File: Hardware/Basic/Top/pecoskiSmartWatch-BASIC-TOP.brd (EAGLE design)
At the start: 38 x 38 mm, 29 parts, among them U2 NRF52832_MODULE_MDBT42

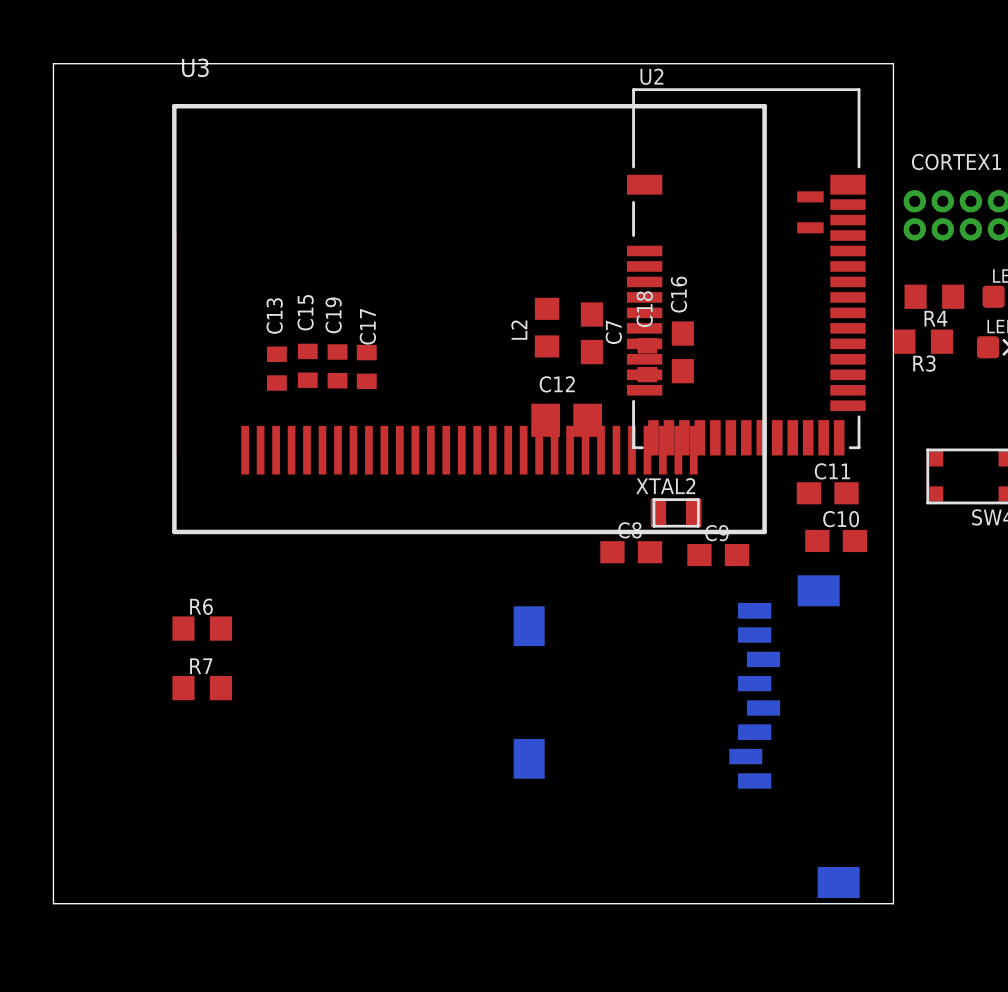
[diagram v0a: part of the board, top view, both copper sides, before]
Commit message: Updated top board hardware Eagle
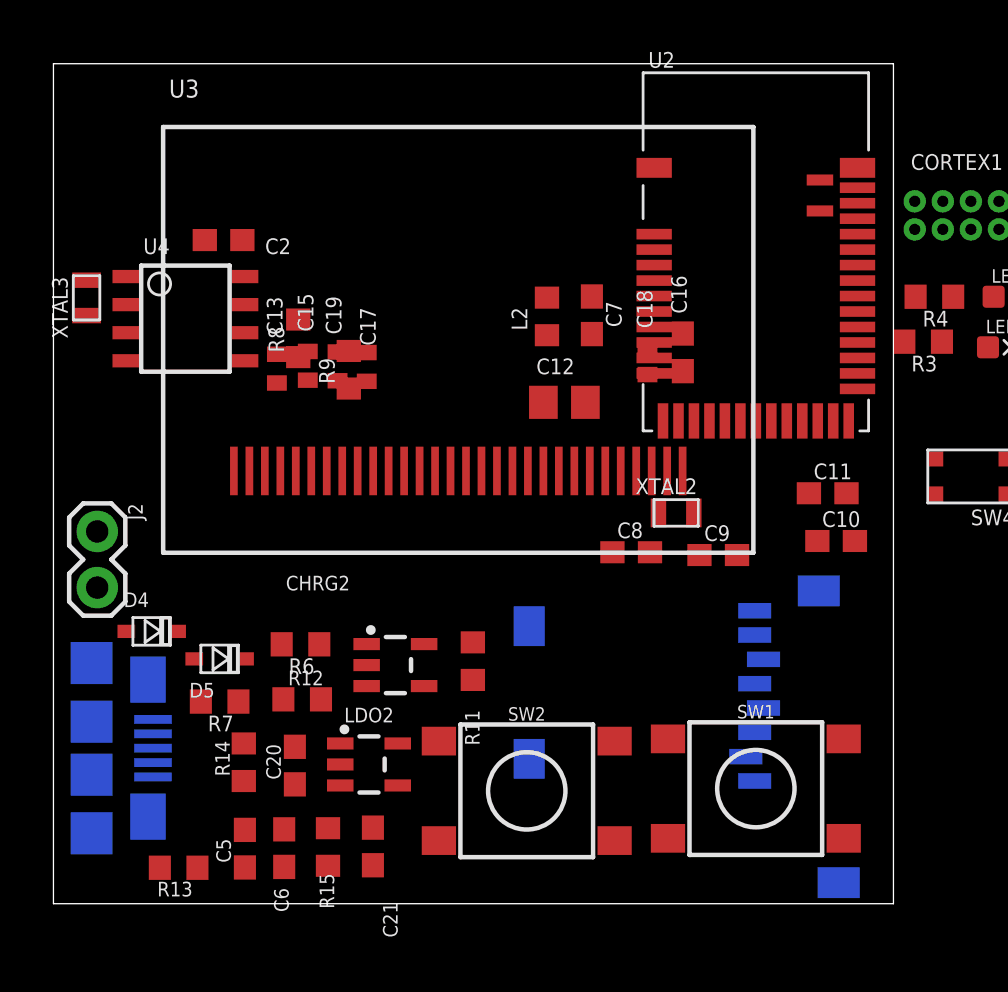
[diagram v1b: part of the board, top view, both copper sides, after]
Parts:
- added C2, C5, C6: 1u, LinnesLab-Passives:C0603
- added C20, C21: 4.7u, LinnesLab-Passives:C0603
- added CHRG2: MCP73831, LinnesLab-Power:SOT23-5
- added D4, D5: (no value), LinnesLab-DiscreteSemi:USC
- added J2: (no value), LinnesLab-Connectors:1X02
- added LDO2: MIC5504, LinnesLab-Power:SOT23-5
- added R11: (no value), LinnesLab-Passives:R0603
- added R12, R13, R14, R15: 100k, LinnesLab-Passives:R0603
- added R8, R9: 10k, LinnesLab-Passives:R0603
- added SW1, SW2: SWITCH.MOM, LinnesLab-Switches:TACTILE_SWITCH_SMD_6.2MM_TALL
- added U4: PCF8523, LinnesLab-Clocks:SO8
- added USB2: USB.MICRO-BIGGERPADS, LinnesLab-Connectors:USB-MICRO-01.BIGGERPADS
- added XTAL3: 32.7680kHz, LinnesLab-Clocks:2-SMD.NOLEAD.2.0MMTO1.2MM
- moved R6 4.50 mm to (11.2, 11.7), turned to 180 degrees
- moved U3 1.07 mm to (18.3, 20.8)
- moved R7 1.00 mm to (7.52, 9.14), turned to 180 degrees
- moved U2 0.88 mm to (31.8, 29.5)
- moved C12 0.82 mm to (23.1, 22.7)
- moved C7 0.81 mm to (24.4, 26.6)
- moved L2 0.51 mm to (22.3, 26.6)
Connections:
- new net BATT: R13.1, R14.2
- new net CHRG.STAT: CHRG2.1, R12.1
- new net N$17: CHRG2.5, R11.2
- new net N$19: U4.2, XTAL3.P$1
- new net N$20: U4.1, XTAL3.P$2
- new net SW1: SW1.A1, SW2.A1
- new net USB+: USB2.3
- new net USB-: USB2.2
- new net VBAT: U4.3
- new net VIN: C21.2, C5.2, CHRG2.4, D4.-, D5.-, LDO2.1, LDO2.3, R12.2
- new net VLIPO: C20.1, CHRG2.3, D4.+, J2.2, R13.2
- new net V_USB: D5.+, USB2.1
- net 3.3V: now also C2.1, C6.1, LDO2.5, R15.2, R8.2, R9.2, U4.8
- net GND: now also C2.2, C20.2, C21.1, C5.1, C6.2, CHRG2.2, J2.1, LDO2.2, R11.1, R14.1, R15.1, SW1.B1, SW1.B2, SW2.B1, SW2.B2, U4.4, USB2.5, USB2.S1, USB2.S2, USB2.S3, USB2.S4, USB2.S5, USB2.S6
- net SCL: now also R8.1, U4.6
- net SDA: now also R9.1, U4.5

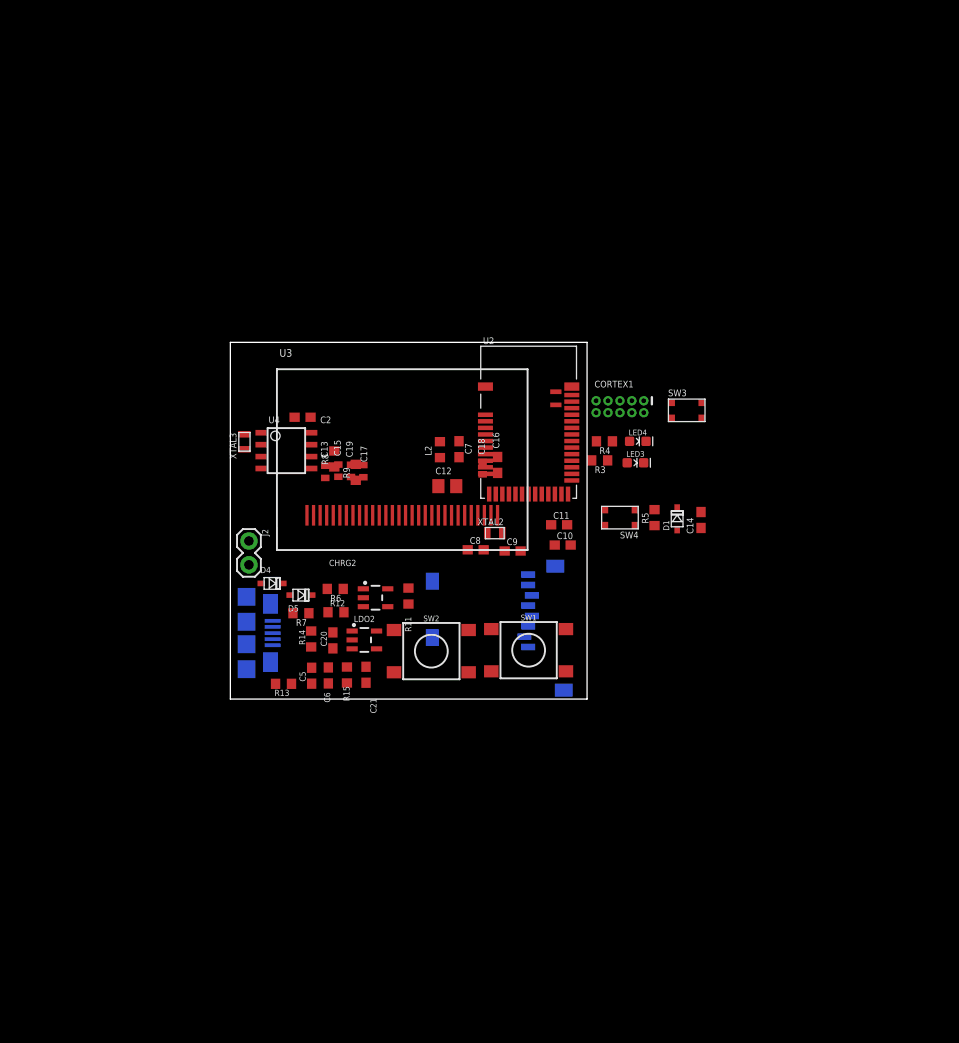
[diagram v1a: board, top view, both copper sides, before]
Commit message: Updated Eagle Hardware 2021_02_27
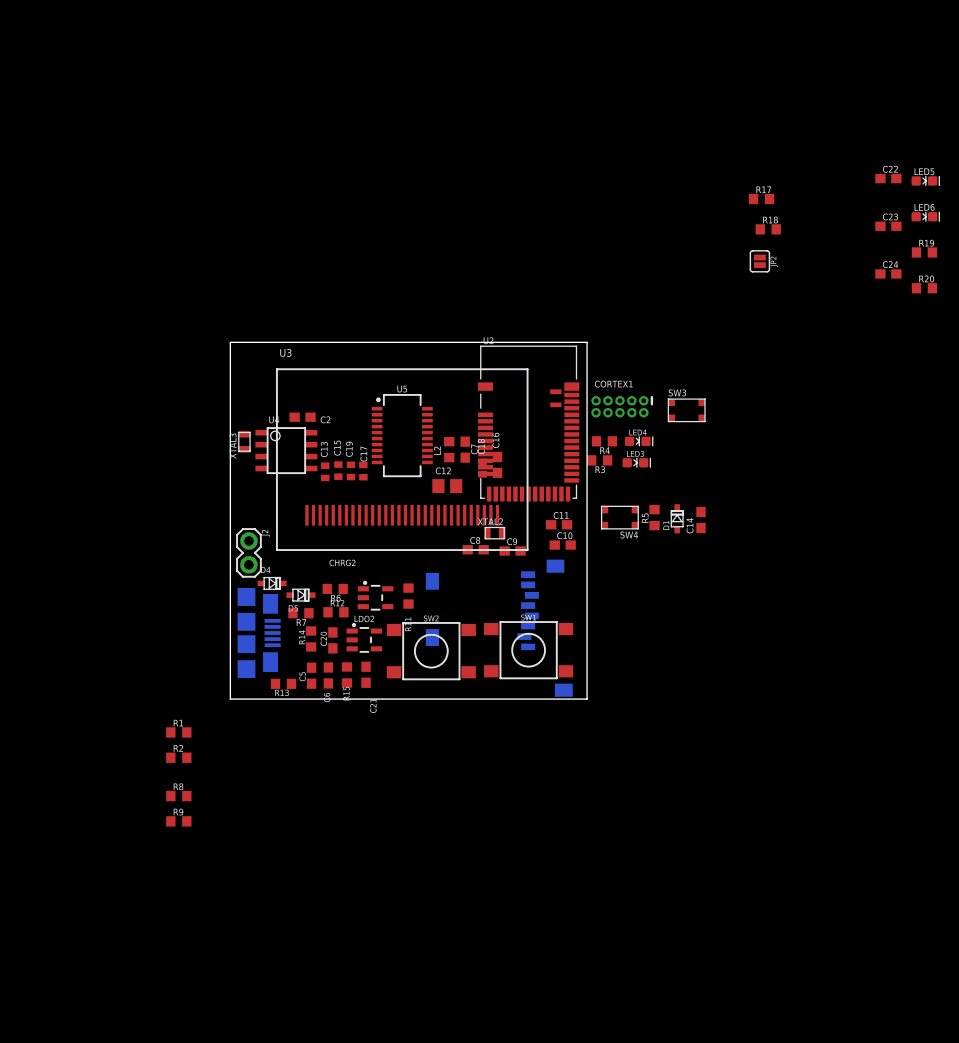
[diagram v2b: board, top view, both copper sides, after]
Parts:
- added C22: 100n, LinnesLab-Passives:C0603
- added C23, C24: 47p, LinnesLab-Passives:C0603
- added JP2: (no value), LinnesLab-Switches:SMT-JUMPER_2_NO_SILK
- added LED5: RED, LinnesLab-LED:LED-0603
- added LED6: YELLOW, LinnesLab-LED:LED-0603
- added R1, R2: 0, LinnesLab-Passives:R0603
- added R17, R18: 27, LinnesLab-Passives:R0603
- added R19, R20: 1k, LinnesLab-Passives:R0603
- added U5: FT231XS, LinnesLab-DigitalIC:SSOP20_L
- moved R9 41.7 mm to (-5.49, -13.0), turned to 0 degrees
- moved R8 39.5 mm to (-5.49, -10.3), turned to 0 degrees
- moved L2 0.99 mm to (23.3, 26.6)
- moved C7 0.66 mm to (25.0, 26.6)
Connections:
- removed net BATT: R13.1, R14.2
- removed net CD1: SD2.CD1
- removed net CHRG.STAT: CHRG2.1, R12.1
- removed net CS.OLED: U3.13
- removed net DC.OLED: U3.15
- removed net RESET.OLED: U3.14
- removed net RXD: U2.21
- removed net SD.CS: SD2.2
- removed net SW1: SW1.A1, SW2.A1
- removed net TXD: U2.19
- new net !CTS: JP2.2, U5.9
- new net !DTR: U5.1
- new net A4/BATT: R13.1, R14.2, U2.5
- new net A6/TIA: U2.7
- new net A7/PPG: U2.8
- new net D11/SW1: SW1.A1, U2.25
- new net D15/SW2: SW2.A1, U2.29
- new net D16/CS.OLED: U2.30, U3.13
- new net D27/CHRG.STATUS: CHRG2.1, R12.1, U2.4
- new net D29/LED.CTRL: U2.6
- new net D3/RESET.OLED: U2.16, U3.14
- new net D4/DC.OLED: U2.17, U3.15
- new net D5/CD1: SD2.CD1, U2.18
- new net D7/SD.CS: SD2.2, U2.20
- new net FT3V3: U5.13
- new net N$23: R17.2, U5.12
- new net N$24: R18.2, U5.11
- new net N$25: LED5.C, R19.2
- new net N$26: LED6.C, R20.2
- new net RXD.FT: R2.1, U5.4
- new net RXD.NRF: R1.2, U2.21
- new net RXLED: R19.1, U5.17
- new net TXD.FT: R1.1, U5.20
- new net TXD.NRF: R2.2, U2.19
- new net TXLED: R20.1, U5.10
- net 3.3V: now also C22.2, LED5.A, LED6.A, U5.14, U5.3
- net GND: now also C22.1, C23.2, C24.1, JP2.1, U5.16, U5.6
- net SCL: now also R9.1; no longer R8.1
- net SDA: now also R8.1; no longer R9.1
- net USB+: now also C23.1, R18.1
- net USB-: now also C24.2, R17.1
- net V_USB: now also U5.15

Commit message: HW Updates 2021/03/06
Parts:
- removed C22: 100n, LinnesLab-Passives:C0603
- removed C23, C24: 47p, LinnesLab-Passives:C0603
- removed CHRG2: MCP73831, LinnesLab-Power:SOT23-5
- removed CORTEX1: CORTEX_DEBUG_PTH, LinnesLab-Connectors:2X5-PTH-1.27MM
- removed D4, D5: (no value), LinnesLab-DiscreteSemi:USC
- removed JP2: (no value), LinnesLab-Switches:SMT-JUMPER_2_NO_SILK
- removed L2: 10u, LinnesLab-Passives:L0603
- removed LDO2: MIC5504, LinnesLab-Power:SOT23-5
- removed LED5: RED, LinnesLab-LED:LED-0603
- removed LED6: YELLOW, LinnesLab-LED:LED-0603
- removed R19, R20: 1k, LinnesLab-Passives:R0603
- removed U5: FT231XS, LinnesLab-DigitalIC:SSOP20_L
- removed XTAL3: 32.7680kHz, LinnesLab-Clocks:2-SMD.NOLEAD.2.0MMTO1.2MM
- added C1: 1u, LinnesLab-Passives:C0603
- added C3: (no value), LinnesLab-Passives:C0603
- added C4: 4.7u, LinnesLab-Passives:C0603
- added CHRG: MCP73831, LinnesLab-Power:SOT23-5
- added D2, D3: (no value), LinnesLab-DiscreteSemi:USC
- added DEBUG1: CORTEX_DEBUG_PTH, LinnesLab-Connectors:2X5-PTH-1.27MM
- added J1: (no value), LinnesLab-Connectors:1X02
- added JP1: (no value), LinnesLab-Switches:SMT-JUMPER_2_NO_SILK
- added L1: 10u, LinnesLab-Passives:L0603
- added LDO1: MIC5504, LinnesLab-Power:SOT23-5
- added LED1: RED, LinnesLab-LED:LED-0603
- added LED2: BLUE, LinnesLab-LED:LED-0603
- added R10: 10k, LinnesLab-Passives:R0603
- added R16: 1k, LinnesLab-Passives:R0603
- added U1: NRF52832_MODULE_MDBT42, LinnesLab-Microcontrollers:BLE_MODULE_RAYTAC_MDBT42
- added XTAL1: 32.768kHz, LinnesLab-Clocks:2-SMD.NOLEAD.2.0MMTO1.2MM
- C10: value 300p -> 4.7u
- C11: value 300p -> 100n
- C12: value 10u -> 47p; device LinnesLab-Passives:C0805 -> LinnesLab-Passives:C0603
- C13: value 2.2uF -> 47p; device LinnesLab-Passives:C0402 -> LinnesLab-Passives:C0603
- C14: value 100n -> 10uF
- C15: value 2.2uF -> 100n; device LinnesLab-Passives:C0402 -> LinnesLab-Passives:C0603
- C16: value 10uF -> 2.2uF; device LinnesLab-Passives:C0603 -> LinnesLab-Passives:C0402
- C2: value 1u -> 10u; device LinnesLab-Passives:C0603 -> LinnesLab-Passives:C0805
- C20: value 4.7u -> 2.2uF; device LinnesLab-Passives:C0603 -> LinnesLab-Passives:C0402
- C21: value 4.7u -> 1u
- C5: value 1u -> (none)
- C7: value 1u -> 300p
- C8: value (none) -> 300p
- C9: value (none) -> 1u
- J2: device LinnesLab-Connectors:1X02 -> LinnesLab-Connectors:1X07_1.27MM
- LED4: value BLUE -> YELLOW
- R1, R2: value 0 -> 10k
- R11: value (none) -> 10k
- R12, R13: value 100k -> 27
- R14: value 100k -> 390k
- R15: value 100k -> 1k
- R17, R18: value 27 -> 0
- R3: value 1k -> 100k
- R4: value 1k -> (none)
- R5, R8, R9: value 10k -> 100k
- R6: value 10k -> 1k
- R7: value 390k -> 1k
- SW1, SW2: value SWITCH.MOM -> (none); device LinnesLab-Switches:TACTILE_SWITCH_SMD_6.2MM_TALL -> LinnesLab-Switches:BUTTON-GULLWING
- SW3, SW4: value (none) -> SWITCH.MOM; device LinnesLab-Switches:BUTTON-GULLWING -> LinnesLab-Switches:TACTILE_SWITCH_SMD_6.2MM_TALL
- U2: value NRF52832_MODULE_MDBT42 -> PCF8523; device LinnesLab-Microcontrollers:BLE_MODULE_RAYTAC_MDBT42 -> LinnesLab-Clocks:SO8
- U3: value (none) -> FT231XS; device LinnesLab-Displays:UG-2864HSWEG01_0.96IN_NO-WRAPAROUND -> LinnesLab-DigitalIC:SSOP20_L
- U4: value PCF8523 -> (none); device LinnesLab-Clocks:SO8 -> LinnesLab-Displays:UG-2864HSWEG01_0.96IN_NO-WRAPAROUND
- XTAL2: value 32.768kHz -> 32.7680kHz
- moved R15 72.0 mm to (47.5, 65.4), turned to 0 degrees
- moved R13 71.4 mm to (47.0, 59.9)
- moved R12 64.0 mm to (47.2, 62.3), turned to 180 degrees
- moved R4 53.5 mm to (12.9, -18.8), turned to 270 degrees
- moved C13 52.6 mm to (49.6, 59.0), turned to 270 degrees
- moved R7 51.3 mm to (57.4, 21.0)
- moved C15 50.0 mm to (37.7, 66.9), turned to 270 degrees
- moved R3 50.0 mm to (11.4, -16.0), turned to 0 degrees
- moved U3 49.7 mm to (41.9, 64.5), turned to 270 degrees
- moved C12 48.4 mm to (49.8, 63.1), turned to 270 degrees
- moved D1 47.9 mm to (8.97, -9.12), turned to 0 degrees
- moved C5 46.6 mm to (55.2, 5.08), turned to 0 degrees
- moved R6 46.6 mm to (57.2, 18.7)
- moved C10 42.0 mm to (14.9, -20.2), turned to 90 degrees
- moved LED4 41.3 mm to (50.9, 68.1), turned to 180 degrees
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- renumbered SD2 to SD1, USB2 to USB1
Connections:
- net !CTS: now also JP1.2, U3.9; no longer JP2.2, U5.9
- net !DTR: now also U3.1; no longer U5.1
- net 3.3V: now also C15.2, C2.2, C20.2, C21.1, C9.1, D3.-, DEBUG1.1, J2.4, LDO1.5, LED3.A, LED4.A, R1.2, R10.2, R2.2, U1.11, U2.8, U3.14, U3.3, U4.6, U4.9; no longer C12.2, C17.2, C2.1, C22.2, C6.1, CORTEX1.1, D1.-, LDO2.5, LED5.A, LED6.A, R15.2, R8.2, R9.2, U2.11, U3.6, U3.9, U4.8, U5.14, U5.3
- net A4/BATT: now also R8.1, R9.2, U1.5; no longer R13.1, R14.2, U2.5
- net A6/TIA: now also J2.6, U1.7; no longer U2.7
- net A7/PPG: now also J2.7, U1.8; no longer U2.8
- net D11/SW1: now also SW3.A1, U1.25; no longer SW1.A1, U2.25
- net D15/SW2: now also SW4.A1, U1.29; no longer SW2.A1, U2.29
- net D16/CS.OLED: now also U1.30, U4.13; no longer U2.30, U3.13
- net D27/CHRG.STATUS: now also CHRG.1, R3.1, U1.4; no longer CHRG2.1, R12.1, U2.4
- net D29/LED.CTRL: now also J2.5, U1.6; no longer U2.6
- net D3/RESET.OLED: now also U1.16, U4.14; no longer U2.16, U3.14
- net D4/DC.OLED: now also U1.17, U4.15; no longer U2.17, U3.15
- net D5/CD1: now also U1.18; no longer U2.18
- net D7/SD.CS: now also U1.20; no longer U2.20
- net DFU: now also SW1.3, U1.34; no longer SW3.3, U2.34
- net DTR: now also C11.1; no longer C14.1
- net FRST: now also U1.38; no longer U2.38
- net FT3V3: now also U3.13; no longer U5.13
- net GND: now also C1.2, C13.2, C14.1, C15.1, C2.1, C20.1, C21.2, C3.1, C4.1, C5.2, C6.1, C8.2, CHRG.2, DEBUG1.3, DEBUG1.5, DEBUG1.7, DEBUG1.9, J1.1, J2.3, JP1.1, LDO1.2, LED1.C, LED2.C, R14.2, R4.1, R5.1, R9.1, SW1.1, SW2.3, SW3.B1, SW3.B2, SW4.B1, SW4.B2, U1.1, U1.12, U1.24, U1.39, U2.4, U3.16, U3.6, U4.1, U4.10, U4.12, U4.29, U4.30, U4.8; no longer C11.2, C16.1, C18.1, C2.2, C20.2, C21.1, C22.1, C23.2, C24.1, C5.1, C6.2, C8.1, CHRG2.2, CORTEX1.3, CORTEX1.5, CORTEX1.7, CORTEX1.9, J2.1, JP2.1, LDO2.2, LED3.C, LED4.C, R14.1, R15.1, R6.1, R7.2, SW1.B1, SW1.B2, SW2.B1, SW2.B2, SW3.1, SW4.3, U2.1, U2.12, U2.24, U2.39, U3.1, U3.10, U3.12, U3.29, U3.30, U3.8, U4.4, U5.16, U5.6
- net LED1: now also R6.2, U1.31; no longer R3.2, U2.31
- net LED2: now also R7.2, U1.33; no longer R4.2, U2.33
- net MISO: now also U1.28; no longer U2.28
- net MOSI: now also U1.27, U4.19; no longer U2.27, U3.19
- net N$1: now also R11.2, U4.11; no longer R6.2, U3.11
- net N$10: now also LED2.A, R7.1; no longer LED4.A, R4.1
- net N$11: now also L1.1, U1.10; no longer L2.1, U2.10
- net N$12: now also C1.1, L1.2, U1.9; no longer C7.1, L2.2, U2.9
- net N$13: now also C14.2, U4.28; no longer C16.2, U3.28
- net N$14: now also DEBUG1.8; no longer CORTEX1.8
- net N$15: now also C17.2, U4.27; no longer C18.2, U3.27
- net N$17: now also CHRG.5, R4.2; no longer CHRG2.5, R11.2
- net N$19: now also U2.2, XTAL2.P$1; no longer U4.2, XTAL3.P$1
- net N$2: now also R14.1, U4.26; no longer R7.1, U3.26
- net N$20: now also U2.1, XTAL2.P$2; no longer U4.1, XTAL3.P$2
- net N$23: now also R12.2, U3.12; no longer R17.2, U5.12
- net N$24: now also R13.2, U3.11; no longer R18.2, U5.11
- net N$25: now also LED3.C, R15.2; no longer LED5.C, R19.2
- net N$26: now also LED4.C, R16.2; no longer LED6.C, R20.2
- net N$3: now also C18.2, U4.2; no longer C13.2, U3.2
- net N$4: now also C3.2, U1.13, XTAL1.P$1; no longer C8.2, U2.13, XTAL2.P$1
- net N$5: now also C18.1, U4.3; no longer C13.1, U3.3
- net N$6: now also C5.1, U1.14, XTAL1.P$2; no longer C9.1, U2.14, XTAL2.P$2
- net N$7: now also C16.2, U4.4; no longer C15.2, U3.4
- net N$8: now also C16.1, U4.5; no longer C15.1, U3.5
- net N$9: now also LED1.A, R6.1; no longer LED3.A, R3.1
- net P0.09/NFC1: now also C7.1, U1.22; no longer C11.1, U2.22
- net P0.10/NFC2: now also C8.1, U1.23; no longer C10.1, U2.23
- net RESET: now also C11.2, D3.+, DEBUG1.10, R10.1, SW2.1, U1.35; no longer C14.2, CORTEX1.10, D1.+, R5.1, SW4.1, U2.35
- net RXD.FT: now also R18.1, U3.4; no longer R2.1, U5.4
- net RXD.NRF: now also R17.2, U1.21; no longer R1.2, U2.21
- net RXLED: now also R15.1, U3.17; no longer R19.1, U5.17
- net SCK: now also U1.26, U4.18; no longer U2.26, U3.18
- net SCL: now also J2.2, R2.1, U1.3, U2.6; no longer R9.1, U2.3, U4.6
- net SDA: now also J2.1, R1.1, U1.2, U2.5; no longer R8.1, U2.2, U4.5
- net SWCLK: now also DEBUG1.4, U1.36; no longer CORTEX1.4, U2.36
- net SWDIO: now also DEBUG1.2, U1.37; no longer CORTEX1.2, U2.37
- net SWO: now also DEBUG1.6, U1.32; no longer CORTEX1.6, U2.32
- net TXD.FT: now also R17.1, U3.20; no longer R1.1, U5.20
- net TXD.NRF: now also R18.2, U1.19; no longer R2.2, U2.19
- net TXLED: now also R16.1, U3.10; no longer R20.1, U5.10
- net USB+: now also C13.1, R13.1; no longer C23.1, R18.1
- net USB-: now also C12.2, R12.1; no longer C24.2, R17.1
- net VBAT: now also U2.3; no longer U4.3
- net VIN: now also C4.2, C6.2, CHRG.4, D1.-, D2.-, LDO1.1, LDO1.3, R3.2; no longer C21.2, C5.2, CHRG2.4, D4.-, D5.-, LDO2.1, LDO2.3, R12.2
- net VLIPO: now also C10.1, CHRG.3, D1.+, J1.2, R8.2; no longer C20.1, CHRG2.3, D4.+, J2.2, R13.2
- net V_USB: now also D2.+, U3.15; no longer D5.+, U5.15
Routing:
- net TXLED: track 0.00 -> 13.7 mm, vias 0 -> 2
- net N$12: track 0.00 -> 7.20 mm
- net RXD.FT: track 0.00 -> 6.92 mm
- net TXD.FT: track 0.00 -> 2.95 mm
- net N$24: track 0.00 -> 2.93 mm
- net N$11: track 0.00 -> 2.16 mm
- net RXLED: track 0.00 -> 2.02 mm
- net GND: track 0.00 -> 1.87 mm, vias 0 -> 1
- net N$25: track 0.00 -> 1.83 mm
- net N$23: track 0.00 -> 1.76 mm
- net N$26: track 0.00 -> 1.75 mm
- net USB-: track 0.00 -> 1.75 mm
- net USB+: track 0.00 -> 1.71 mm

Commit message: HW Updates 2021/03/06 Pt 2
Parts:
- removed C7, C8: 300p, LinnesLab-Passives:C0603
- removed R5: 100k, LinnesLab-Passives:R0603
- removed XTAL2: 32.7680kHz, LinnesLab-Clocks:2-SMD.NOLEAD.2.0MMTO1.2MM
- added Y2: 32.7680kHz, LinnesLab-Clocks:2-SMD.NOLEAD.2.0MMTO1.2MM
- moved C15 82.5 mm to (-22.0, 9.98)
- moved R15 82.5 mm to (-12.3, 8.52)
- moved C12 82.5 mm to (-9.91, 6.20)
- moved JP1 82.5 mm to (-14.7, -11.9)
- moved R12 82.5 mm to (-12.5, 5.36)
- moved R13 82.5 mm to (-12.7, 2.97)
- moved R17 82.5 mm to (-14.3, 13.4)
- moved U3 82.5 mm to (-17.8, 7.57)
- moved LED3 82.2 mm to (-8.77, 9.03)
- moved R16 82.2 mm to (-12.0, 11.2)
- moved LED4 82.1 mm to (-8.31, 11.2)
- moved C13 81.9 mm to (-10.1, 2.80)
- moved R18 81.8 mm to (-18.6, 13.7)
- moved R14 52.7 mm to (31.6, 17.5), turned to 0 degrees
- moved R11 48.6 mm to (15.6, 22.5), turned to 270 degrees
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- renumbered XTAL1 to Y1
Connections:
- net 3.3V: no longer R5.2
- net GND: no longer C7.2, C8.2, R5.1
- net N$19: now also Y2.P$1; no longer XTAL2.P$1
- net N$20: now also Y2.P$2; no longer XTAL2.P$2
- net P0.09/NFC1: no longer C7.1
- net P0.10/NFC2: no longer C8.1
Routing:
- net GND: track 1.87 -> 27.8 mm, vias 1 -> 14
- net VLIPO: track 0.00 -> 13.0 mm
- net TXLED: track 13.7 -> 1.60 mm, vias 2 -> 1
- net VIN: track 0.00 -> 7.99 mm
- net N$2: track 0.00 -> 6.63 mm
- net N$13: track 0.00 -> 5.38 mm
- net N$5: track 0.00 -> 4.56 mm
- net N$8: track 0.00 -> 3.99 mm
- net N$15: track 0.00 -> 3.87 mm
- net N$3: track 0.00 -> 2.98 mm
- net N$12: track 7.20 -> 4.26 mm
- net N$1: track 0.00 -> 2.49 mm
- net 3.3V: track 0.00 -> 2.35 mm, vias 0 -> 1
- net V_USB: track 0.00 -> 2.16 mm
- net N$7: track 0.00 -> 2.14 mm
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- added copper zone on layer 1, net 3.3V
- added copper zone on layer 16, net GND

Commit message: Updated HW 2021_03_13 AM
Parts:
- removed SD1: (no value), LinnesLab-Connectors:MICROSD
- moved C11 56.8 mm to (2.61, 25.6), turned to 180 degrees
- moved R9 56.1 mm to (2.00, 20.3)
- moved D3 52.7 mm to (2.88, 27.5), turned to 0 degrees
- moved R2 52.7 mm to (12.9, 36.3)
- moved R8 51.7 mm to (3.91, 20.3), turned to 270 degrees
- moved R10 50.2 mm to (2.64, 29.7), turned to 0 degrees
- moved C21 50.0 mm to (56.7, 40.6)
- moved U2 50.0 mm to (54.9, 37.1)
- moved Y2 50.0 mm to (50.4, 38.2)
- moved R1 48.8 mm to (9.06, 36.3)
- moved SW2 47.1 mm to (2.59, 33.2), turned to 90 degrees
- moved C10 33.6 mm to (9.64, 12.9), flipped to the bottom, turned to 0 degrees
- moved R4 32.4 mm to (4.81, 12.6), flipped to the bottom, turned to 180 degrees
- moved CHRG 27.2 mm to (9.53, 9.88), flipped to the bottom, turned to 180 degrees
- moved R3 25.8 mm to (12.1, 9.80), flipped to the bottom, turned to 270 degrees
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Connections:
- removed net CD2: SD1.CD2
- net 3.3V: no longer SD1.4
- net D5/CD1: no longer SD1.CD1
- net D7/SD.CS: no longer SD1.2
- net GND: no longer SD1.6, SD1.MT1, SD1.MT2
- net MISO: no longer SD1.7
- net MOSI: no longer SD1.3
- net SCK: no longer SD1.5
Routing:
- net USB-: track 1.75 -> 23.8 mm, vias 0 -> 1
- net USB+: track 2.08 -> 17.1 mm, vias 0 -> 1
- net VLIPO: track 13.0 -> 25.0 mm
- net VIN: track 7.99 -> 16.0 mm
- net N$2: track 6.63 -> 0.00 mm
- net RXD.FT: track 6.38 -> 0.00 mm
- net GND: track 27.8 -> 34.1 mm, vias 14 -> 15
- net N$13: track 5.38 -> 0.00 mm
- net N$17: track 0.00 -> 5.28 mm
- net N$15: track 3.87 -> 0.02 mm
- net N$4: track 0.00 -> 1.99 mm
- net A4/BATT: track 0.00 -> 1.91 mm
- net TXLED: track 1.60 -> 0.00 mm, vias 1 -> 0
- net SWDIO: track 0.00 -> 1.39 mm, vias 0 -> 1
- net V_USB: track 2.16 -> 2.66 mm
